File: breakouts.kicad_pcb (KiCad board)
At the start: 2 copper layers, 239 x 117.5 mm, 163 parts, among them IC901 ATTINY85-S, J1101 USB_MINI-B, J1201 JACK_5P, J201 USB_MINI-B, J301 USB_MINI-B, J401 SMA, J801 USB_MINI-B, K1201 CONN_3, K1301 CONN_3, K601 CONN_3, K801 CONN_3, P1001 CONN_4, P1002 CONN_4, P1101 CONN_6, P1102 CONN_6, P1201 CONN_2, P1202 CONN_2, P1203 CONN_2, P1301 CONN_2, P201 CONN_2, P202 CONN_2, P203 CONN_2, P301 CONN_6, P302 CONN_6, P401 CONN_8, P402 CONN_8, P501 CONN_2, P502 CONN_2, P701 POWER, P702 PORT B, P703 PORT C, P704 PORT D, P705 ISP, P801 PORT B, P802 PORT C, P803 PORT D, P804 ISP, P901 CONN_8, P902 ISP, SW701 SW_PUSH, SW801 SW_PUSH, SW901 SW_PUSH, U1001 SST25VF016B, U1101 FT230X-QFN, U1201 TDA1517ATW, U1301 MCP7940M, U301 FT230X, U401 MRF49XA, U501 SP6641A/B, U601 NX1117C33Z, U701 ATMEGA88PA-A, U801 ATMEGA32U2, X1301 32.768kHz, X401 10MHz, X701 12MHz 18pF, X801 16MHz 18pF

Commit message: breakaway placement
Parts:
- added breakaway: VAL**, breakaway, F.Cu at (98.8, 123.2)
- added breakaway: VAL**, breakaway, F.Cu at (29.7, 105.3)
- added breakaway: VAL**, breakaway, F.Cu at (44.7, 105.3)
- added slot-10mm: VAL**, slot-10mm, F.Cu at (52.2, 105.3)
- added slot-10mm: VAL**, slot-10mm, F.Cu at (91.3, 123.2)
- added slot-10mm: VAL**, slot-10mm, F.Cu at (106.3, 123.2)
- added slot-10mm: VAL**, slot-10mm, F.Cu at (37.2, 105.3)
- added slot-5mm: VAL**, slot-5mm, F.Cu at (56.0, 107.0)
- moved C1102 175.2 mm to (48.0, 84.4)
- moved C1105 175.2 mm to (31.7, 84.4)
- moved D1102 175.2 mm to (31.7, 81.1)
- moved P1101 175.2 mm to (27.9, 85.2)
- moved R1102 175.2 mm to (31.7, 78.8)
- moved C1101 175.2 mm to (45.4, 84.4)
- moved C1103 175.2 mm to (36.8, 92.8)
- moved C1104 175.2 mm to (41.4, 92.8)
- moved D1101 175.2 mm to (46.7, 81.1)
- moved J1101 175.2 mm to (39.1, 99.4)
- moved P1102 175.2 mm to (50.8, 85.2)
- moved R1101 175.2 mm to (46.7, 78.8)
- moved R1103 175.2 mm to (33.0, 92.6)
- moved R1104 175.2 mm to (40.6, 89.0)
- moved R1105 175.2 mm to (37.6, 89.0)
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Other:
- outline, holes or cut-outs redrawn

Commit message: slots and breakaways
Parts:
- removed the breakaway at (56.0, 142.0)
- removed the slot-10mm at (52.2, 105.3)
- added breakaway: VAL**, breakaway, F.Cu at (112.9, 119.9)
- added breakaway: VAL**, breakaway, F.Cu at (56.0, 138.6)
- added breakaway: VAL**, breakaway, F.Cu at (40.7, 76.4)
- added breakaway: VAL**, breakaway, F.Cu at (56.0, 108.6)
- added breakaway: VAL**, breakaway, F.Cu at (56.0, 66.8)
- added breakaway: VAL**, breakaway, F.Cu at (56.0, 102.0)
- added breakaway: VAL**, breakaway, F.Cu at (33.5, 105.3)
- added breakaway: VAL**, breakaway, F.Cu at (78.5, 105.3)
- added breakaway: VAL**, breakaway, F.Cu at (108.5, 105.3)
- added breakaway: VAL**, breakaway, F.Cu at (87.0, 133.6)
- added breakaway: VAL**, breakaway, F.Cu at (105.3, 123.2)
- added breakaway: VAL**, breakaway, F.Cu at (112.9, 141.5)
- added breakaway: VAL**, breakaway, F.Cu at (112.9, 109.9)
- added breakaway: VAL**, breakaway, F.Cu at (107.9, 66.1)
- added breakaway: VAL**, breakaway, F.Cu at (87.0, 118.6)
- added slot-10mm: VAL**, slot-10mm, F.Cu at (86.0, 105.3)
- added slot-10mm: VAL**, slot-10mm, F.Cu at (87.0, 126.1)
- added slot-10mm: VAL**, slot-10mm, F.Cu at (97.8, 123.2)
- added slot-10mm: VAL**, slot-10mm, F.Cu at (112.8, 123.2)
- added slot-10mm: VAL**, slot-10mm, F.Cu at (112.9, 134.0)
- added slot-10mm: VAL**, slot-10mm, F.Cu at (136.3, 115.1)
- added slot-5mm: VAL**, slot-5mm, F.Cu at (112.9, 114.9)
- moved P1201 186.2 mm to (65.4, 67.5), turned to 180 degrees
- moved P1202 179.0 mm to (73.0, 67.5), turned to 180 degrees
- moved P401 174.5 mm to (101.5, 79.4), turned to 180 degrees
- moved J1201 174.0 mm to (53.7, 94.4), turned to 0 degrees
- moved C1202 173.5 mm to (63.2, 82.5), turned to 270 degrees
- moved P1203 171.9 mm to (80.8, 67.5), turned to 180 degrees
- moved C1204 170.7 mm to (72.2, 76.2), turned to 90 degrees
- moved X401 167.2 mm to (93.7, 88.5), turned to 270 degrees
- moved C403 165.2 mm to (112.3, 82.6), turned to 0 degrees
- moved L401 164.6 mm to (107.9, 84.5), turned to 180 degrees
- moved U401 163.2 mm to (100.3, 88.5), turned to 270 degrees
- moved C1205 161.6 mm to (70.8, 86.8), turned to 270 degrees
- moved D902 161.2 mm to (31.8, 65.6), turned to 90 degrees
- moved C405 160.5 mm to (106.0, 88.3), turned to 90 degrees
- moved BMIS-203_Shield 160.3 mm to (103.1, 89.6), turned to 270 degrees
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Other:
- board size 239 x 117.5 mm -> 100 x 100 mm

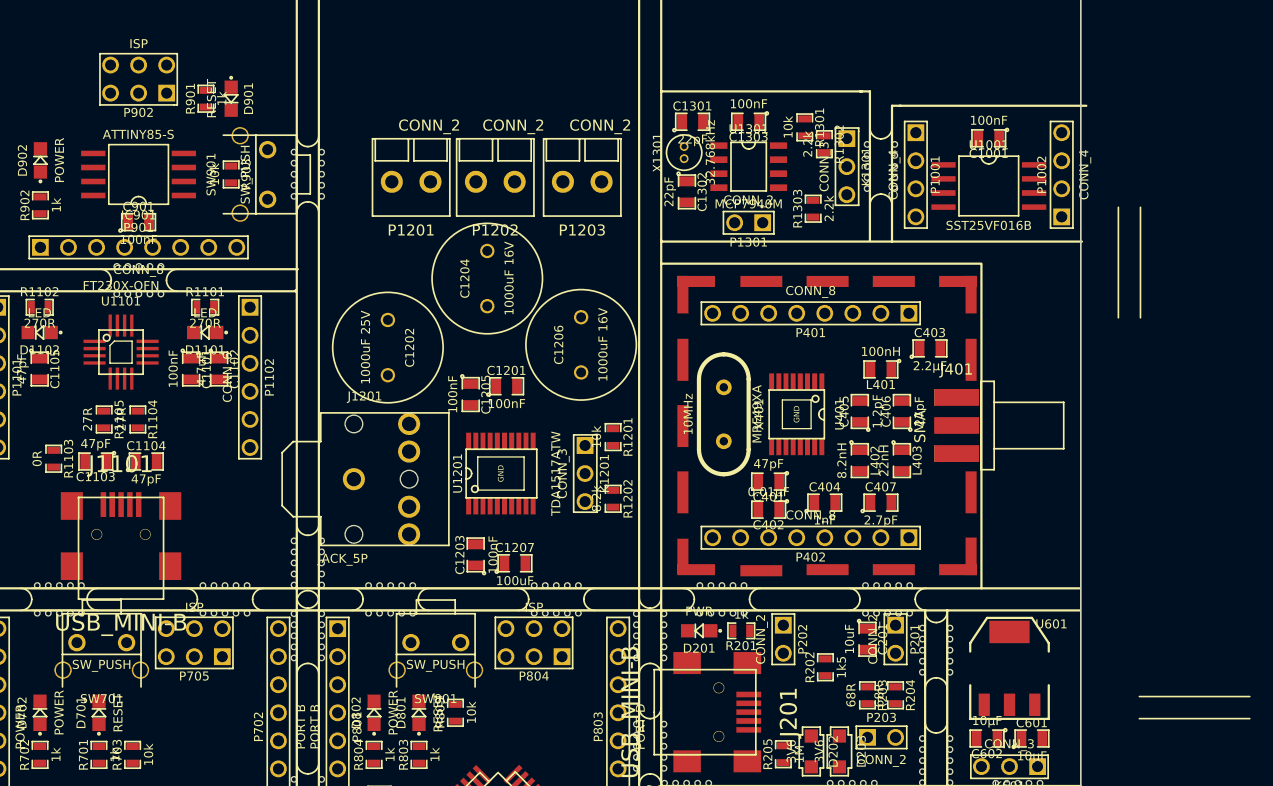
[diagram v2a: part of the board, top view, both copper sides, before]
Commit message: breakaway and slots placement
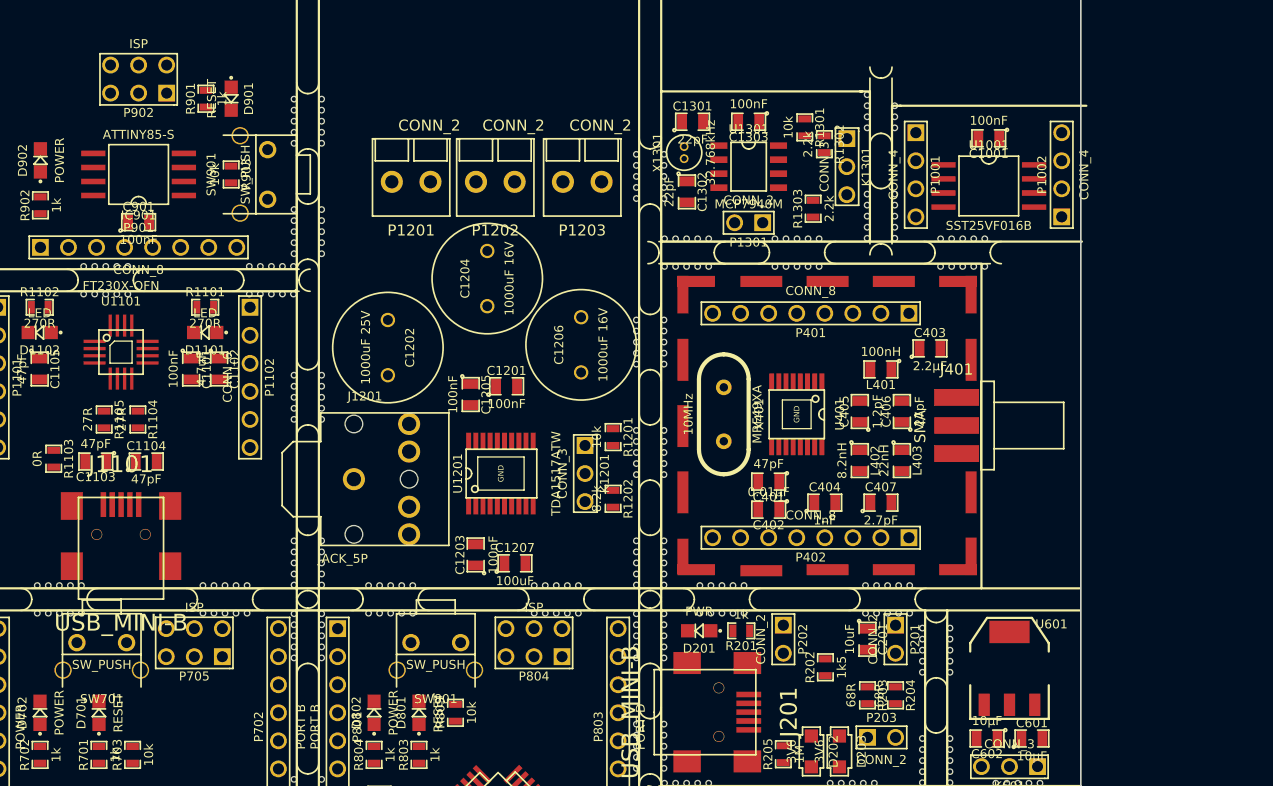
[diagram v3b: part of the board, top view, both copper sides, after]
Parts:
- added breakaway: VAL**, breakaway, F.Cu at (87.0, 102.0)
- added breakaway: VAL**, breakaway, F.Cu at (87.0, 82.0)
- added breakaway: VAL**, breakaway, F.Cu at (90.3, 73.9)
- added breakaway: VAL**, breakaway, F.Cu at (87.0, 92.0)
- added breakaway: VAL**, breakaway, F.Cu at (87.0, 67.0)
- added breakaway: VAL**, breakaway, F.Cu at (100.3, 73.9)
- added breakaway: VAL**, breakaway, F.Cu at (115.3, 73.9)
- added breakaway: VAL**, breakaway, F.Cu at (107.9, 60.6)
- added breakaway: VAL**, breakaway, F.Cu at (56.0, 87.0)
- added breakaway: VAL**, breakaway, F.Cu at (37.7, 76.4)
- added breakaway: VAL**, breakaway, F.Cu at (56.0, 62.0)
- added slot-10mm: VAL**, slot-10mm, F.Cu at (87.0, 74.5)
- added slot-10mm: VAL**, slot-10mm, F.Cu at (107.8, 73.9)
- added slot-10mm: VAL**, slot-10mm, F.Cu at (56.0, 79.5)
- added slot-10mm: VAL**, slot-10mm, F.Cu at (45.2, 76.4)
- added slot-5mm: VAL**, slot-5mm, F.Cu at (87.0, 97.0)
- added slot-5mm: VAL**, slot-5mm, F.Cu at (87.0, 87.0)
- added slot-5mm: VAL**, slot-5mm, F.Cu at (95.3, 73.9)
- added slot-5mm: VAL**, slot-5mm, F.Cu at (107.9, 65.6)
- added slot-5mm: VAL**, slot-5mm, F.Cu at (56.0, 67.0)
- moved slot-10mm 82.9 mm to (56.0, 94.5), turned to 90 degrees
- moved slot-10mm 47.7 mm to (87.0, 94.5)
- moved breakaway 12.0 mm to (52.7, 76.4)
- moved breakaway 5.20 mm to (56.0, 72.0)
- moved breakaway 4.50 mm to (107.9, 70.6)

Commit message: Board edges
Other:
- board size 100 x 100 mm -> 100 x 92.6 mm
